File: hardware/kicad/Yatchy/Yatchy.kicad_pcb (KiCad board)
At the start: 4 copper layers, 33.8 x 38 mm, 90 parts, among them IC2 MCP23018-E_MJ, IC3 MCP73831T-2ATI_OT, J1 MOD_CONN, J10 MOD_CONN, J11 MOD_CONN, J12 MOD_CONN, J13 MOD_CONN, J14 MOD_CONN, J15 MOD_CONN, J16 MOD_CONN, J19 MOD_CONN, J2 MOD_CONN, J20 MOD_CONN, J21 MOD_CONN, J22 MOD_CONN, J23 MOD_CONN, J24 MOD_CONN, J25 MOD_CONN, J26 Conn_01x03_Pin, J27 MOD_CONN, J28 Conn_01x02_Pin, J3 MOD_CONN, J4 USB4730-GF-A-KIT, J5 SFV24R-4STBE1HLF, J6 MOD_CONN, J7 MOD_CONN, J8 MOD_CONN, J9 MOD_CONN, M1 Vibration_Motor, Q1 AO3400A, Q4 FDN304PZ, Q5 BC817-25.215, SW1 EVP-AKE31A, SW2 EVP-AKE31A, SW3 EVP-AKE31A, U2 TLV75533PDBV, U3 ESP32-C6-MINI-1-N4, Y2 32.768KHz

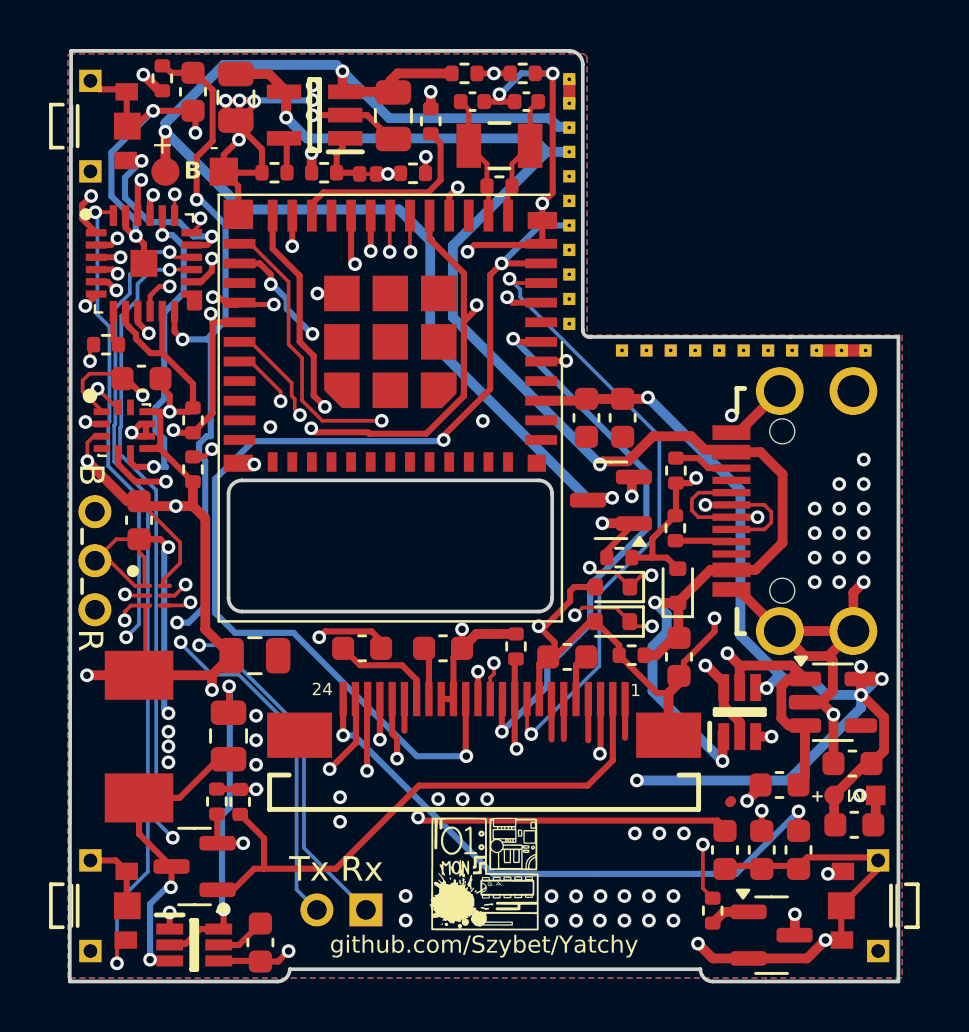
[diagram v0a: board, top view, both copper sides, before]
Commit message: Add screen, expose test point
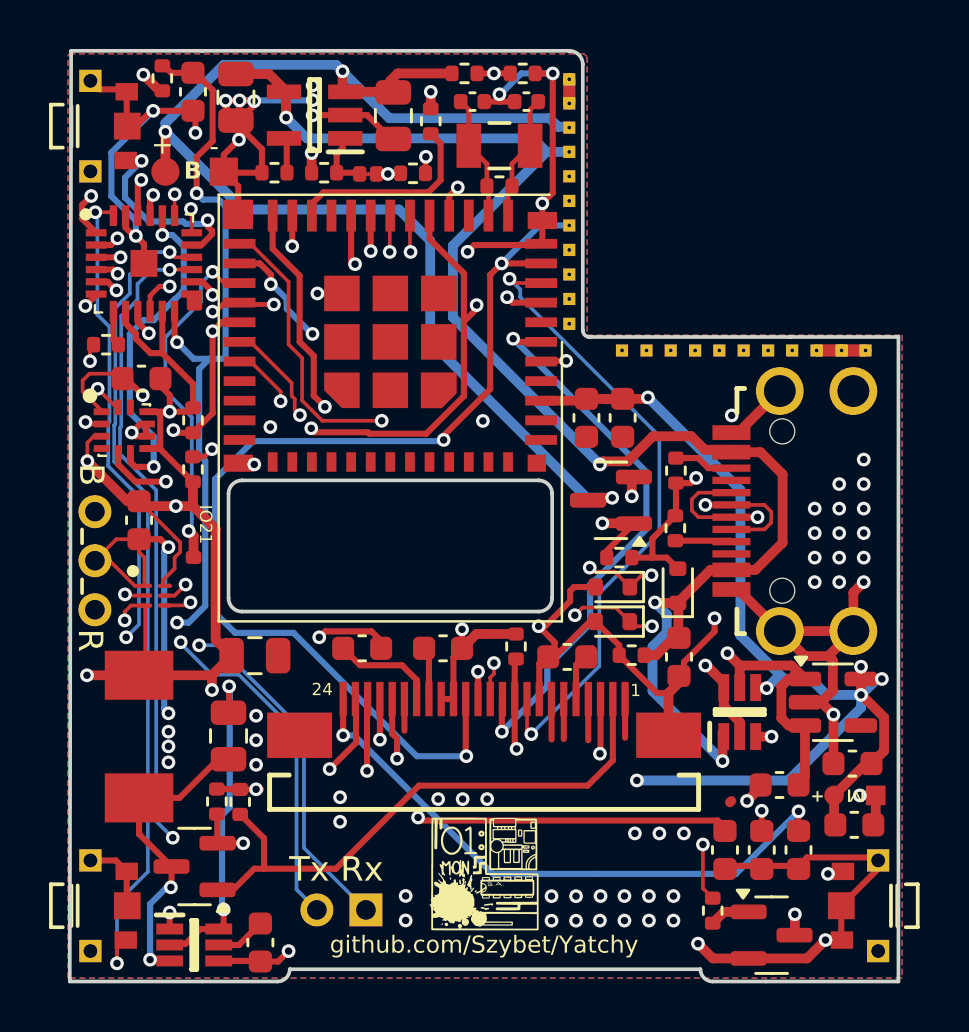
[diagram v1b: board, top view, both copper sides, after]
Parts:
- added J17: Conn_01x01_Pin, Yatchy:testpoint, F.Cu at (71.7, 95.0)
- added REF**: screen, Yatchy:screen, B.Cu at (83.6, 92.9)
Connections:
- U3 pad 27: unconnected-(U3-IO21-Pad27) -> Net-(J17-Pin_1)
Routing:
- net Net-(J17-Pin_1): track 0.00 -> 14.3 mm, vias 0 -> 2
- net EN: track 49.7 -> 50.8 mm
- net MOD_CS: track 26.6 -> 27.7 mm
- net BTN_4: track 40.9 -> 41.6 mm
- net SDA: track 44.6 -> 44.0 mm
- net SCL: track 46.9 -> 46.4 mm
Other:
- board text added: "IO21"
- board text added: "Yatchy"
- board text added: "v1.4"

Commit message: fix dfm and screen footprint
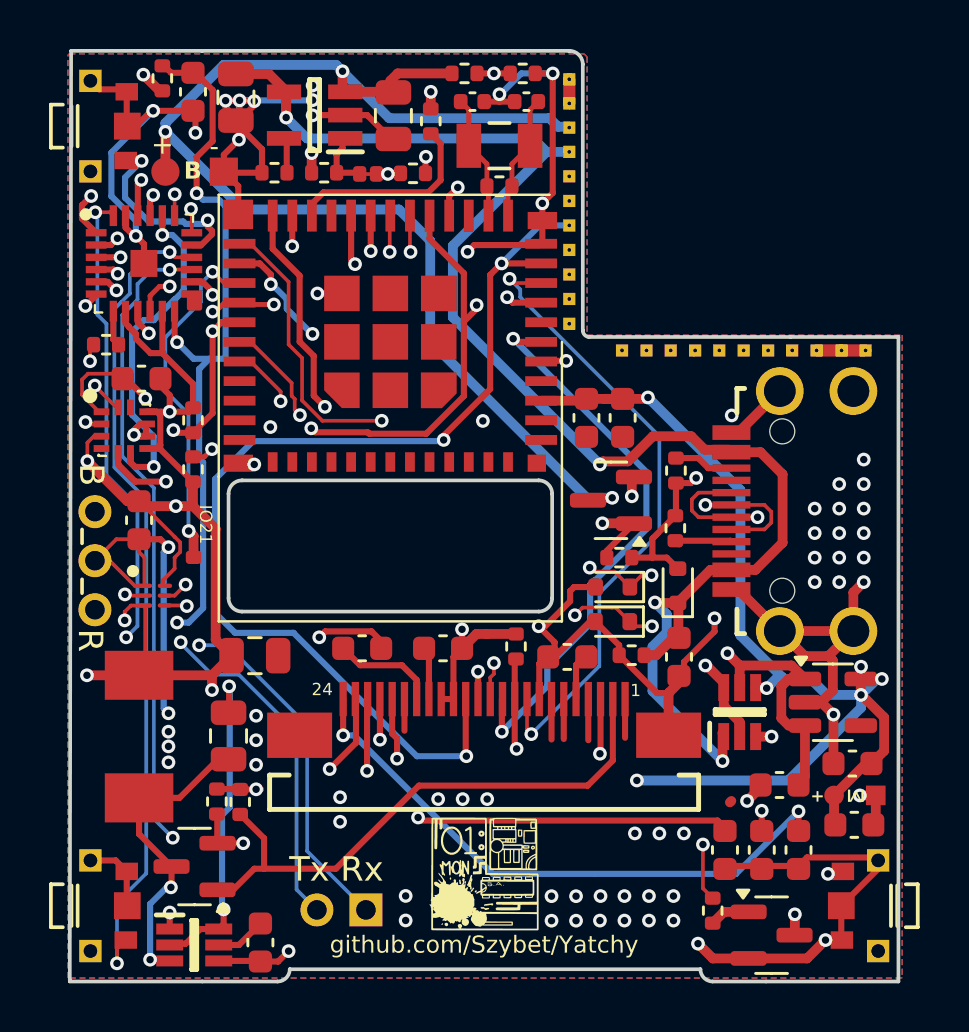
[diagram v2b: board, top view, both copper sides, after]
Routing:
- net GND: track 203.1 -> 204.2 mm

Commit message: Add silkscreen
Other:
- board text added: "Yatchy v1.4"
- board text added: "https://discord.gg/6PUmRXZRGD"
- board text removed: "Yatchy"
- board text removed: "v1.4"

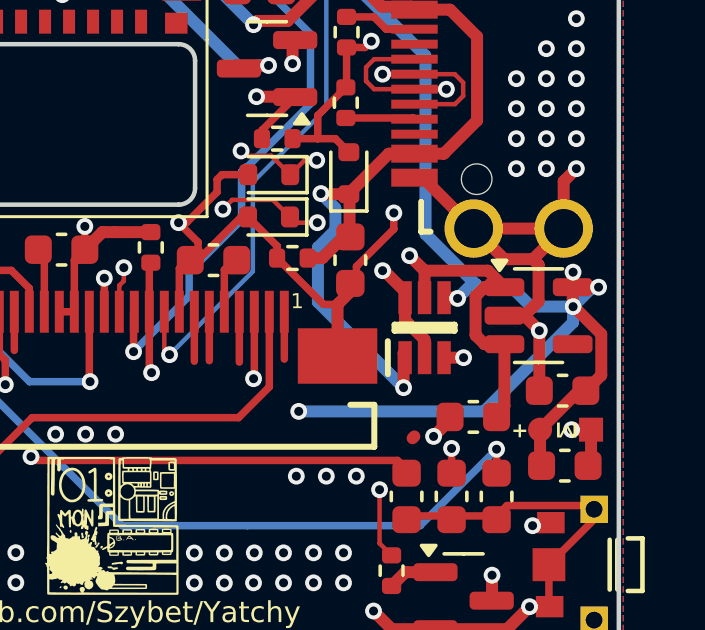
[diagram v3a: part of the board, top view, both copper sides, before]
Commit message: add thermal pad voltage regulator
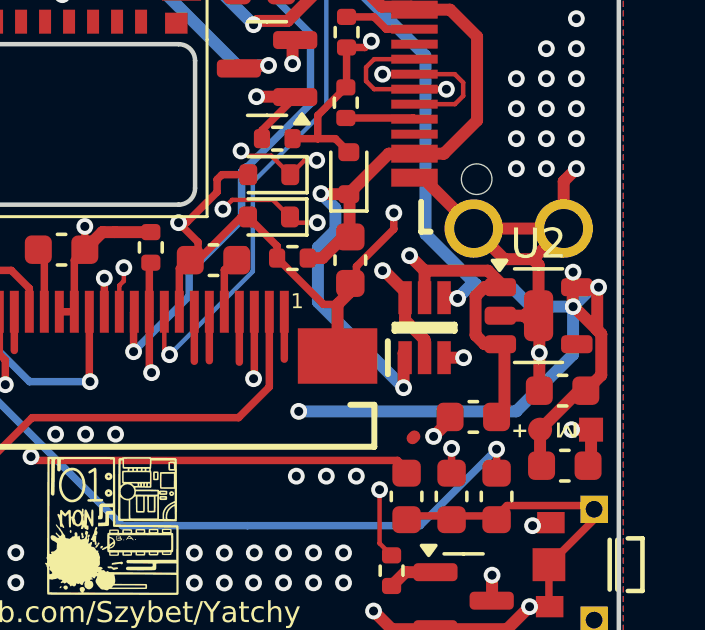
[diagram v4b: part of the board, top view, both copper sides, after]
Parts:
- U2: footprint Package_TO_SOT_SMD:SOT-23-5 -> Yatchy:TLV75733PDYDR
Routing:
- net +3V3: track 133.6 -> 135.8 mm

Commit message: 1.5
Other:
- board text added: "Yatchy v1.5"
- board text removed: "Yatchy v1.4"
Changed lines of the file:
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@@
 		)
 	)
-	(gr_text "Yatchy v1.4"
+	(gr_text "Yatchy v1.5"
 		(at 99.51 109.95 0)
 		(layer "B.SilkS")
